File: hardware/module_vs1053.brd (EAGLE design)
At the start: 109.9 x 68.6 mm, 118 parts, among them IC1 IC_USBLC6-2, IC2 LM1117IMPX-3.3, IC3 PIC32MX795F512, IC4 DP83848, IC5 LM1117MPX-2.5, J1 AUDIO_JACK_TRRSSMD_RA, U1 USD-SOCKETUSD, U3 VS1053-L, X2 CRYSTALS-NOGND-CFPX-217, X3 KUSBVX, Y3 CRYSTAL-GROUNDEDSMD-5X3.2

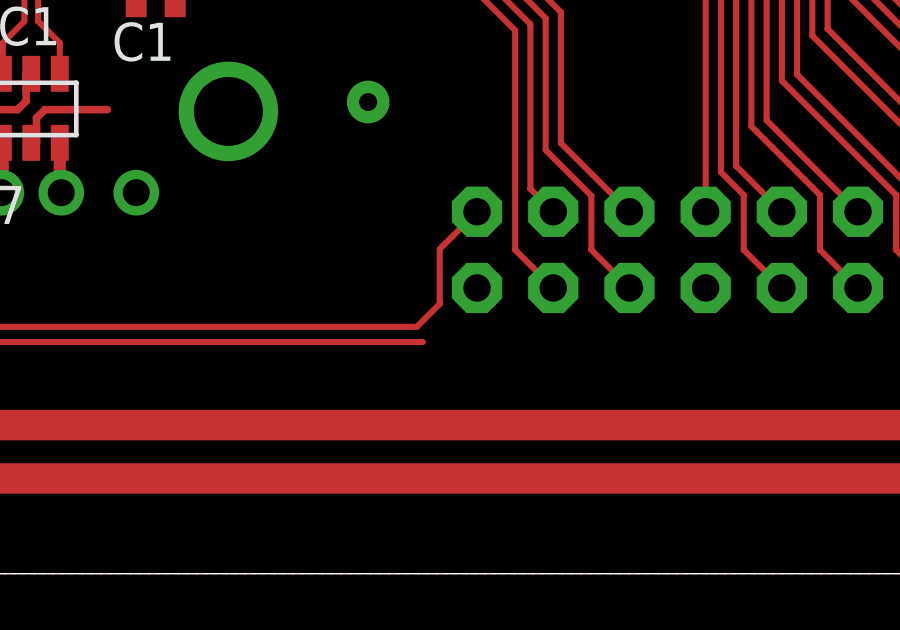
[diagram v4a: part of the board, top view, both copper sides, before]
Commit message: PCB broken line fixed
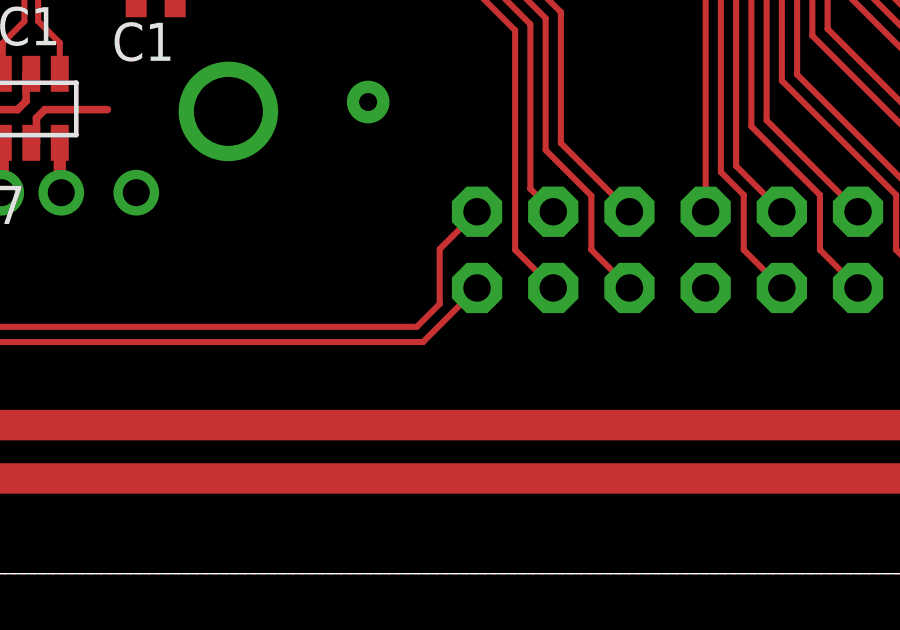
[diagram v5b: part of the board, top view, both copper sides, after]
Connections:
- removed net RF2: IC3.52
- net RF2_ROT_SW: now also IC3.52
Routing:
- net RF2_ROT_SW: track 0.00 -> 47.4 mm
- net RF2: track 44.8 -> 0.00 mm
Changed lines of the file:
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@@
 <wire x1="61.849" y1="10.795" x2="63.119" y2="9.525" width="0.2032" layer="1"/>
-</signal>
-<signal name="RF2">
-<contactref element="IC3" pad="52"/>
-<wire x1="45.892" y1="32.6938" x2="45.892" y2="31.6934" width="0.2032" layer="1"/>
-<wire x1="45.892" y1="31.6934" x2="42.1132" y2="27.9146" width="0.2032" layer="1"/>
-<wire x1="40.5384" y1="13.3858" x2="40.5384" y2="8.7122" width="0.2032" layer="1"/>
-<wire x1="40.5384" y1="8.7122" x2="41.529" y2="7.7216" width="0.2032" layer="1"/>
-<wire x1="41.529" y1="7.7216" x2="58.7756" y2="7.7216" width="0.2032" layer="1"/>
-<wire x1="42.1132" y1="14.9606" x2="40.5384" y2="13.3858" width="0.2032" layer="1"/>
-<wire x1="42.1132" y1="27.9146" x2="42.1132" y2="14.9606" width="0.2032" layer="1"/>
 </signal>
 <signal name="SDA1">
@@
 <signal name="RF2_ROT_SW">
 <contactref element="SV1" pad="2"/>
+<contactref element="IC3" pad="52"/>
+<wire x1="45.892" y1="32.6938" x2="45.892" y2="31.6934" width="0.2032" layer="1"/>
+<wire x1="45.892" y1="31.6934" x2="42.1132" y2="27.9146" width="0.2032" layer="1"/>
+<wire x1="40.5384" y1="13.3858" x2="40.5384" y2="8.7122" width="0.2032" layer="1"/>
+<wire x1="40.5384" y1="8.7122" x2="41.529" y2="7.7216" width="0.2032" layer="1"/>
+<wire x1="41.529" y1="7.7216" x2="58.7756" y2="7.7216" width="0.2032" layer="1"/>
+<wire x1="42.1132" y1="14.9606" x2="40.5384" y2="13.3858" width="0.2032" layer="1"/>
+<wire x1="42.1132" y1="27.9146" x2="42.1132" y2="14.9606" width="0.2032" layer="1"/>
+<wire x1="58.7756" y1="7.7216" x2="60.579" y2="9.525" width="0.2032" layer="1"/>
 </signal>
 </signals>

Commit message: Board optimized for SDR (work in progress)
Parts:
- L2: device dp_devices:FB805 -> rcl:0204/7
- moved C52 9.35 mm to (57.6, 56.2)
- moved C51 8.47 mm to (71.7, 62.8)
- moved IC5 8.35 mm to (68.6, 56.5)
- moved C54 8.35 mm to (62.9, 57.9)
- moved C53 8.35 mm to (62.9, 52.8)
- moved L2 5.31 mm to (80.0, 43.2), flipped to the bottom, turned to 90 degrees
- moved C15 2.98 mm to (66.5, 64.3), turned to 90 degrees
- moved R36 0.64 mm to (80.0, 42.5)
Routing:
- net 3V: track 533.0 -> 525.4 mm, vias 13 -> 12
- net VS_CVDD: track 38.8 -> 35.1 mm
- net _1V8: track 30.3 -> 26.6 mm
- net VS_DREQ: track 45.2 -> 47.0 mm
- net VBUS: track 189.9 -> 188.1 mm
- net VS_MISO: track 92.0 -> 90.9 mm

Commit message: Minor updates in PCB design
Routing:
- net 3V: track 525.4 -> 524.4 mm
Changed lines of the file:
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@@
 <contactref element="SV1" pad="34"/>
 <contactref element="SV1" pad="33"/>
-<wire x1="81.9912" y1="23.4188" x2="85.725" y2="19.685" width="1.016" layer="1"/>
-<wire x1="85.725" y1="19.685" x2="89.5096" y2="19.685" width="1.016" layer="1"/>
-<wire x1="89.5096" y1="19.685" x2="100.965" y2="19.685" width="1.016" layer="1"/>
-<wire x1="100.965" y1="19.685" x2="101.219" y2="19.685" width="1.016" layer="1"/>
+<wire x1="81.9912" y1="24.0538" x2="85.09" y2="20.955" width="1.016" layer="1"/>
 <wire x1="98.425" y1="3.175" x2="101.219" y2="5.969" width="1.016" layer="1"/>
-<wire x1="101.219" y1="12.065" x2="101.219" y2="19.431" width="1.016" layer="1"/>
 <wire x1="101.219" y1="9.525" x2="101.219" y2="5.969" width="1.016" layer="1"/>
 <wire x1="101.219" y1="9.525" x2="101.219" y2="12.065" width="1.016" layer="1"/>
 <wire x1="22.8346" y1="10.1828" x2="22.8346" y2="3.175" width="0.6096" layer="1"/>
-<wire x1="89.4588" y1="19.7358" x2="89.5096" y2="19.685" width="0.251459375" layer="1"/>
-<wire x1="81.9912" y1="30.9626" x2="81.9912" y2="23.4188" width="1.016" layer="1"/>
+<wire x1="81.9912" y1="30.9626" x2="81.9912" y2="24.0538" width="1.016" layer="1"/>
 <wire x1="104.8258" y1="37.882" x2="104.8258" y2="40.6146" width="0.251459375" layer="1"/>
 <wire x1="104.8258" y1="37.882" x2="104.8258" y2="24.5618" width="1.016" layer="1"/>
-<wire x1="101.219" y1="19.431" x2="100.965" y2="19.685" width="1.016" layer="1"/>
 <wire x1="99.7338" y1="40.882" x2="100.2538" y2="41.402" width="0.251459375" layer="1"/>
 <wire x1="100.2538" y1="41.402" x2="104.0384" y2="41.402" width="0.251459375" layer="1"/>
@@
 <wire x1="81.9912" y1="30.9626" x2="79.4512" y2="30.9626" width="1.016" layer="16"/>
 <wire x1="79.4512" y1="30.9626" x2="76.6572" y2="33.7566" width="1.016" layer="16"/>
-<wire x1="101.219" y1="19.685" x2="101.219" y2="20.955" width="1.016" layer="1"/>
 <wire x1="101.219" y1="20.955" x2="104.8258" y2="24.5618" width="1.016" layer="1"/>
 <wire x1="84.8106" y1="42.291" x2="81.3562" y2="45.7454" width="0.6096" layer="16"/>
@@
 <wire x1="63.754" y1="59.344" x2="76.6572" y2="46.4408" width="1.016" layer="16"/>
 <wire x1="76.6572" y1="46.4408" x2="76.6572" y2="45.7454" width="1.016" layer="16"/>
+<wire x1="101.219" y1="12.065" x2="101.219" y2="20.955" width="1.016" layer="1"/>
+<wire x1="101.219" y1="20.955" x2="85.09" y2="20.955" width="1.016" layer="1"/>
 </signal>
 <signal name="SOSCI">
@@
 <wire x1="62.9142" y1="54.1542" x2="62.9158" y2="54.1558" width="1.016" layer="1"/>
 <via x="80.4672" y="32.9184" extent="1-16" drill="0.6" diameter="1.4224" shape="octagon"/>
-<wire x1="80.4672" y1="32.9184" x2="80.4672" y2="22.4028" width="1.016" layer="1"/>
+<wire x1="80.4672" y1="32.9184" x2="80.4672" y2="23.0378" width="1.016" layer="1"/>
 <wire x1="78.3082" y1="35.0774" x2="80.4672" y2="32.9184" width="1.016" layer="16"/>
 <contactref element="SV1" pad="32"/>
 <contactref element="SV1" pad="31"/>
-<wire x1="80.4672" y1="22.4028" x2="85.09" y2="17.78" width="1.016" layer="1"/>
-<wire x1="85.09" y1="17.78" x2="98.679" y2="17.78" width="1.016" layer="1"/>
+<wire x1="80.4672" y1="23.0378" x2="84.455" y2="19.05" width="1.016" layer="1"/>
+<wire x1="84.455" y1="19.05" x2="98.679" y2="19.05" width="1.016" layer="1"/>
 <wire x1="98.679" y1="12.065" x2="98.679" y2="15.24" width="1.016" layer="1"/>
-<wire x1="98.679" y1="15.24" x2="98.679" y2="17.78" width="1.016" layer="1"/>
+<wire x1="98.679" y1="15.24" x2="98.679" y2="19.05" width="1.016" layer="1"/>
 <wire x1="98.679" y1="9.525" x2="98.679" y2="12.065" width="1.016" layer="1"/>
 <wire x1="98.679" y1="9.525" x2="98.679" y2="6.477" width="1.016" layer="1"/>

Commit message: ADC (work in progress)
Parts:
- added C61, C62: 10n, rcl:C0603
- added C63, C64: 1u, rcl:C0603
- added JP1: (no value), pinhead:1X03
- added R12, R37: 470, rcl:0204/5
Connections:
- new net IN_LEFT: C63.2, JP1.2
- new net IN_RIGHT: C64.2, JP1.1
- new net N$13: C62.2, R12.2, U3.1
- new net N$14: C64.1, R37.1
- new net N$15: C63.1, R12.1
- new net N$5: C61.2, R37.2, U3.48
- net VS_AGND: now also C61.1, C62.1, JP1.3
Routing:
- net VS_AGND: track 54.1 -> 49.3 mm
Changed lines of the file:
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@@
 <attribute name="PROD_ID" value="CONN-10676" x="88.9" y="68.58" size="1.778" layer="27" rot="R270" display="off"/>
 </element>
+<element name="C61" library="rcl" package="C0603" value="10n" x="85.725" y="45.72"/>
+<element name="C62" library="rcl" package="C0603" value="10n" x="86.233" y="44.196"/>
+<element name="R12" library="rcl" package="0204/5" value="470" x="78.74" y="57.785" rot="MR270"/>
+<element name="R37" library="rcl" package="0204/5" value="470" x="76.2" y="57.785" rot="MR270"/>
+<element name="C63" library="rcl" package="C0603" value="1u" x="78.74" y="62.865" rot="R90"/>
+<element name="C64" library="rcl" package="C0603" value="1u" x="76.2" y="62.865" rot="R90"/>
+<element name="JP1" library="pinhead" package="1X03" value="" x="78.74" y="66.04" rot="MR180"/>
 </elements>
 <signals>
@@
 <wire x1="92.19" y1="45.327" x2="92.575" y2="45.327" width="0.251459375" layer="1"/>
 <wire x1="92.575" y1="45.327" x2="92.69" y2="45.212" width="0.251459375" layer="1"/>
-<contactref element="R25" pad="1"/>
-<wire x1="87.5928" y1="48.9204" x2="87.5928" y2="47.407" width="0.4064" layer="1"/>
 <contactref element="C36" pad="1"/>
 <contactref element="C39" pad="1"/>
@@
 <wire x1="98.4876" y1="46.5446" x2="98.171" y2="46.228" width="0.251459375" layer="1"/>
 <wire x1="98.171" y1="46.228" x2="95.377" y2="46.228" width="0.251459375" layer="1"/>
-<wire x1="87.5928" y1="48.9204" x2="84.3416" y2="48.9204" width="0.4064" layer="1"/>
 <wire x1="84.3416" y1="50.4444" x2="84.3416" y2="53.467" width="0.6096" layer="1"/>
 <contactref element="R34" pad="2"/>
@@
 <contactref element="U3" pad="47"/>
 <contactref element="J1" pad="EARTH"/>
+<contactref element="JP1" pad="3"/>
+<contactref element="C61" pad="1"/>
+<contactref element="R25" pad="1"/>
+<contactref element="C62" pad="1"/>
+<wire x1="84.3416" y1="60.9736" x2="81.28" y2="66.04" width="0" layer="19" extent="1-1"/>
+<wire x1="84.875" y1="45.72" x2="84.3144" y2="47.8536" width="0" layer="19" extent="1-1"/>
+<wire x1="85.383" y1="44.196" x2="84.875" y2="45.72" width="0" layer="19" extent="1-1"/>
 </signal>
 <signal name="VS_CVDD">
@@
 <wire x1="58.7756" y1="7.7216" x2="60.579" y2="9.525" width="0.2032" layer="1"/>
 </signal>
+<signal name="N$5">
+<contactref element="C61" pad="2"/>
+<contactref element="R37" pad="2"/>
+<contactref element="U3" pad="48"/>
+<wire x1="88.69" y1="44.382" x2="86.575" y2="45.72" width="0" layer="19" extent="1-1"/>
+<wire x1="76.2" y1="55.245" x2="86.575" y2="45.72" width="0" layer="19" extent="1-1"/>
+</signal>
+<signal name="N$13">
+<contactref element="C62" pad="2"/>
+<contactref element="R12" pad="2"/>
+<contactref element="U3" pad="1"/>
+<wire x1="87.083" y1="44.196" x2="78.74" y2="55.245" width="0" layer="19" extent="1-1"/>
+<wire x1="87.19" y1="42.882" x2="87.083" y2="44.196" width="0" layer="19" extent="1-1"/>
+</signal>
+<signal name="N$14">
+<contactref element="R37" pad="1"/>
+<contactref element="C64" pad="1"/>
+<wire x1="76.2" y1="60.325" x2="76.2" y2="62.015" width="0" layer="19" extent="1-1"/>
+</signal>
+<signal name="N$15">
+<contactref element="R12" pad="1"/>
+<contactref element="C63" pad="1"/>
+<wire x1="78.74" y1="60.325" x2="78.74" y2="62.015" width="0" layer="19" extent="1-1"/>
+</signal>
+<signal name="IN_LEFT">
+<contactref element="JP1" pad="2"/>
+<contactref element="C63" pad="2"/>
+<wire x1="78.74" y1="63.715" x2="78.74" y2="66.04" width="0" layer="19" extent="1-1"/>
+</signal>
+<signal name="IN_RIGHT">
+<contactref element="C64" pad="2"/>
+<contactref element="JP1" pad="1"/>
+<wire x1="76.2" y1="63.715" x2="76.2" y2="66.04" width="0" layer="19" extent="1-1"/>
+</signal>
 </signals>
